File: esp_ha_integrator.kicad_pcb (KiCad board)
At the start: 2 copper layers, 68.6 x 30.5 mm, 11 parts, among them J1 DC Regulated 5V SMPS, J2 WS2812, Q1 2N7000, U1 ESP8266-01/ESP-01, U2 AMS1117-3.3

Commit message: updated board and created mill_drill folder
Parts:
- added REF**: MountingHole_2.2mm_M2, MountingHole:MountingHole_2.2mm_M2, F.Cu at (120.4, 87.9)
- added REF**: MountingHole_2.2mm_M2, MountingHole:MountingHole_2.2mm_M2, F.Cu at (157.7, 95.0)
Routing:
- net GND: track 82.8 -> 20.0 mm
- net +5V: track 58.5 -> 64.5 mm
- net +3V3: track 35.0 -> 40.1 mm

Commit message: add copper fill on top
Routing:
- added copper zone on F.Cu, net +3V3
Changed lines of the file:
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@@
       (net 2 "GND") (pinfunction "GND") (pintype "power_in"))
     (pad "2" smd rect (at -3.15 0) (size 2 1.5) (layers "F.Cu" "F.Paste" "F.Mask")
-      (pinfunction "VO") (pintype "power_out"))
+      (net 1 "+3V3") (pinfunction "VO") (pintype "power_out"))
     (pad "2" smd rect (at 3.15 0) (size 2 3.8) (layers "F.Cu" "F.Paste" "F.Mask")
       (net 1 "+3V3") (pinfunction "VO") (pintype "power_out"))
@@
   (segment (start 160.02 86.36) (end 152.4 86.36) (width 0.4) (layer "B.Cu") (net 5))
   (segment (start 148.082 96.52) (end 144.78 96.52) (width 0.4) (layer "B.Cu") (net 5))
+  (zone (net 1) (net_name "+3V3") (layer "F.Cu") (hatch edge 0.508)
+    (connect_pads (clearance 0.508))
+    (min_thickness 0.4) (filled_areas_thickness no)
+    (fill yes (thermal_gap 0.508) (thermal_bridge_width 0.508))
+    (polygon
+      (pts
+        (xy 181.102 104.648)
+        (xy 111.506 104.648)
+        (xy 111.506 73.66)
+        (xy 181.102 72.644)
+      )
+    )
+  )
   (zone (net 2) (net_name "GND") (layer "B.Cu") (hatch edge 0.508)
     (connect_pads (clearance 0.508))

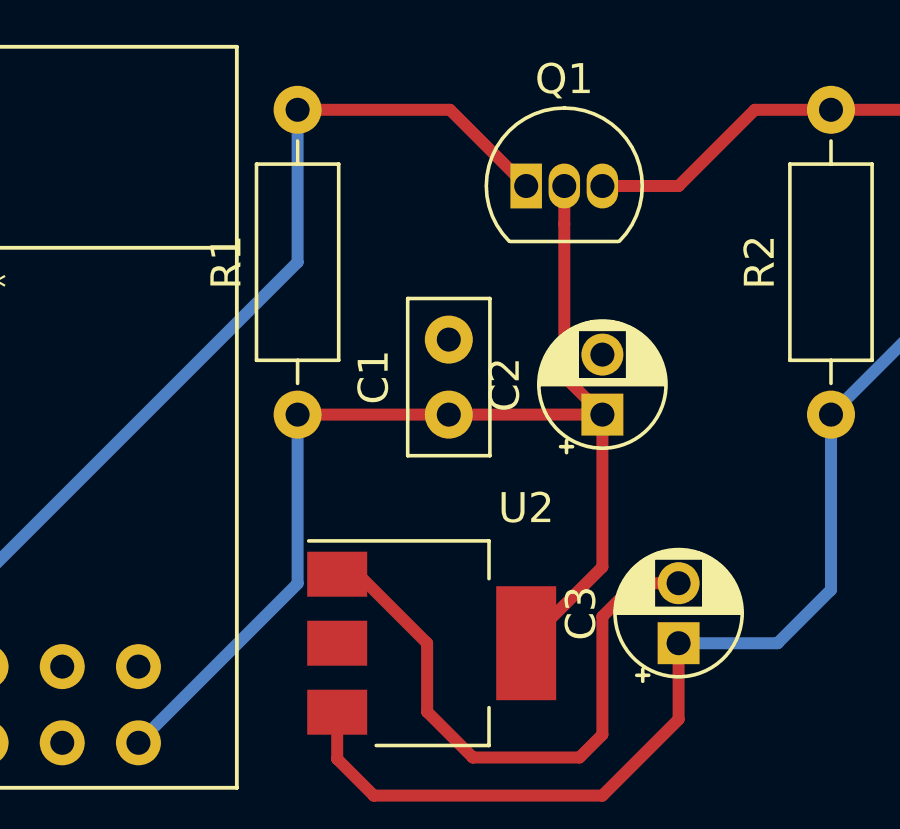
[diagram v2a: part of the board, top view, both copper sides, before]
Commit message: update 3v3 net traces
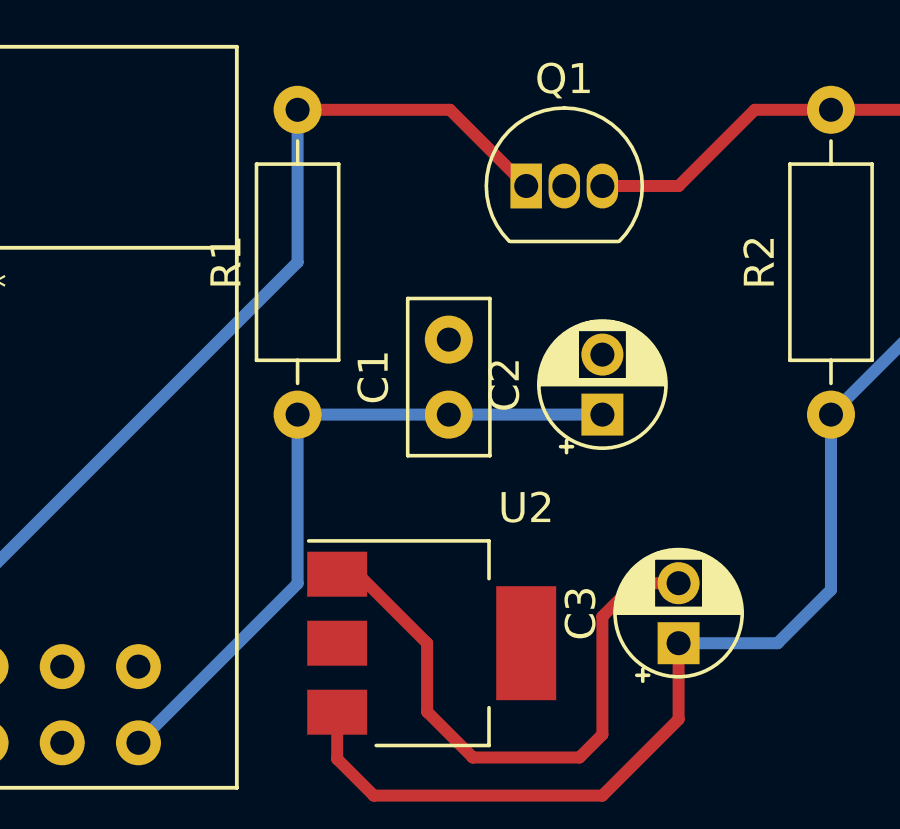
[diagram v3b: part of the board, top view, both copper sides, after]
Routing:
- net +3V3: track 40.1 -> 23.3 mm
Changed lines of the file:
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@@
   (gr_line (start 111.76 73.66) (end 111.76 104.14) (layer "Edge.Cuts") (width 0.1))
   (gr_line (start 111.76 104.14) (end 180.34 104.14) (layer "Edge.Cuts") (width 0.1))
-  (segment (start 137.12 88.9) (end 132.08 88.9) (width 0.4) (layer "F.Cu") (net 1))
-  (segment (start 142.24 88.9) (end 142.24 93.98) (width 0.4) (layer "F.Cu") (net 1))
-  (segment (start 140.97 82.55) (end 140.97 87.63) (width 0.4) (layer "F.Cu") (net 1))
-  (segment (start 142.24 88.9) (end 137.12 88.9) (width 0.4) (layer "F.Cu") (net 1))
-  (segment (start 140.97 81.28) (end 140.97 82.55) (width 0.4) (layer "F.Cu") (net 1))
-  (segment (start 142.24 93.98) (end 139.7 96.52) (width 0.4) (layer "F.Cu") (net 1))
-  (segment (start 140.97 87.63) (end 142.24 88.9) (width 0.4) (layer "F.Cu") (net 1))
   (segment (start 126.775 99.84) (end 132.08 94.535) (width 0.4) (layer "B.Cu") (net 1))
   (segment (start 132.08 94.535) (end 132.08 88.9) (width 0.4) (layer "B.Cu") (net 1))
+  (segment (start 142.24 88.9) (end 137.12 88.9) (width 0.4) (layer "B.Cu") (net 1))
+  (segment (start 132.08 88.9) (end 137.12 88.9) (width 0.4) (layer "B.Cu") (net 1))
   (segment (start 137.922 100.33) (end 141.478 100.33) (width 0.4) (layer "F.Cu") (net 2))
   (segment (start 142.24 95.631) (end 143.351 94.52) (width 0.4) (layer "F.Cu") (net 2))
